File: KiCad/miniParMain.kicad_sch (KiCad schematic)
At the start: 37 parts, among them J1 Conn_01x08, J2 USB_C_Receptacle, J4 Conn_01x02_Pin, J5 secondBoard, SW2 SW_Push, U1 AS7341-DLGT, U2 IP4234CZ6, U5 AP7312-1833W6-7, U8 ESP8685, Y2 40MHz

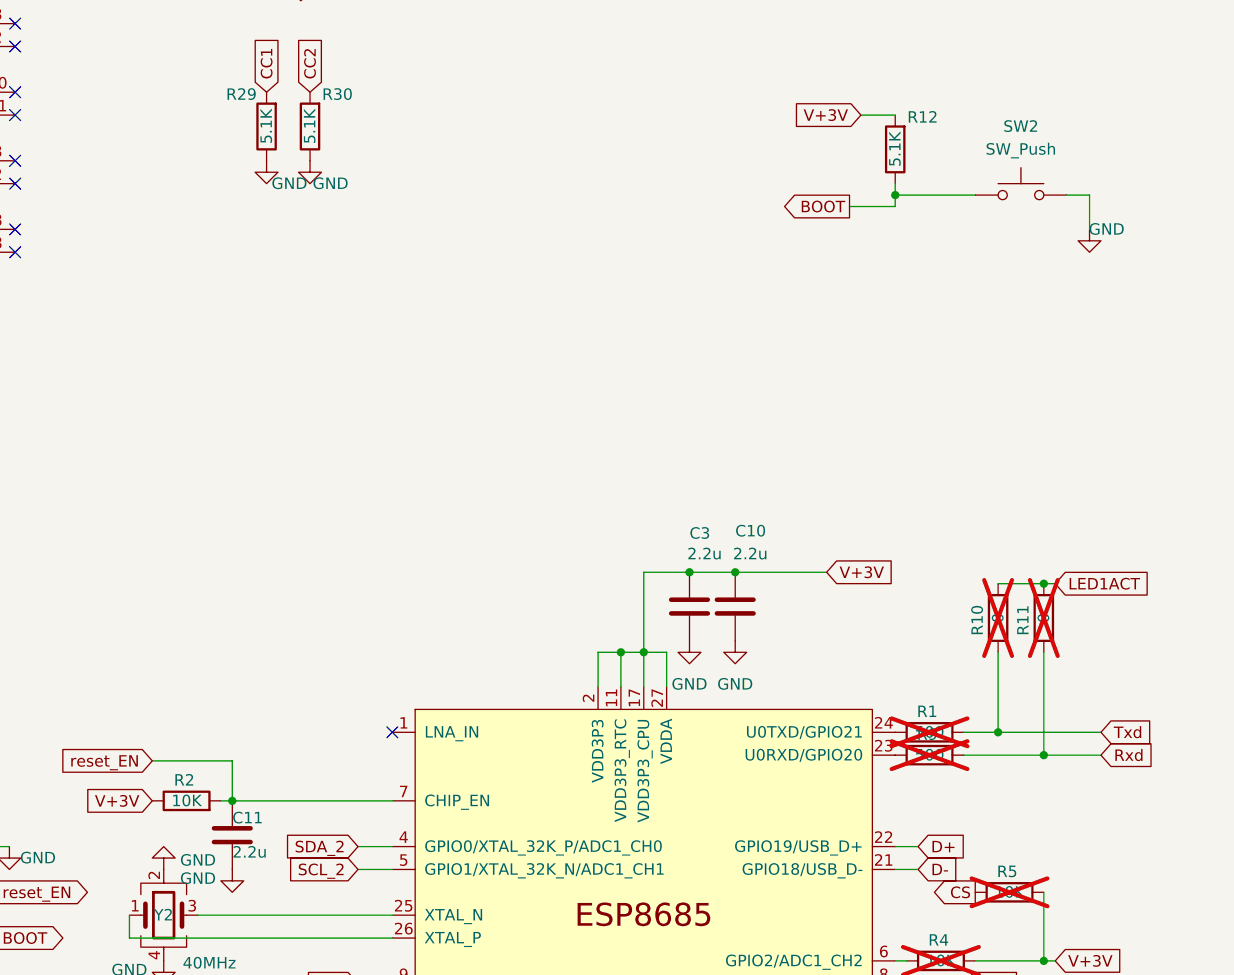
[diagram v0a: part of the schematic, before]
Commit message: clean up of schematics - mpn + bom
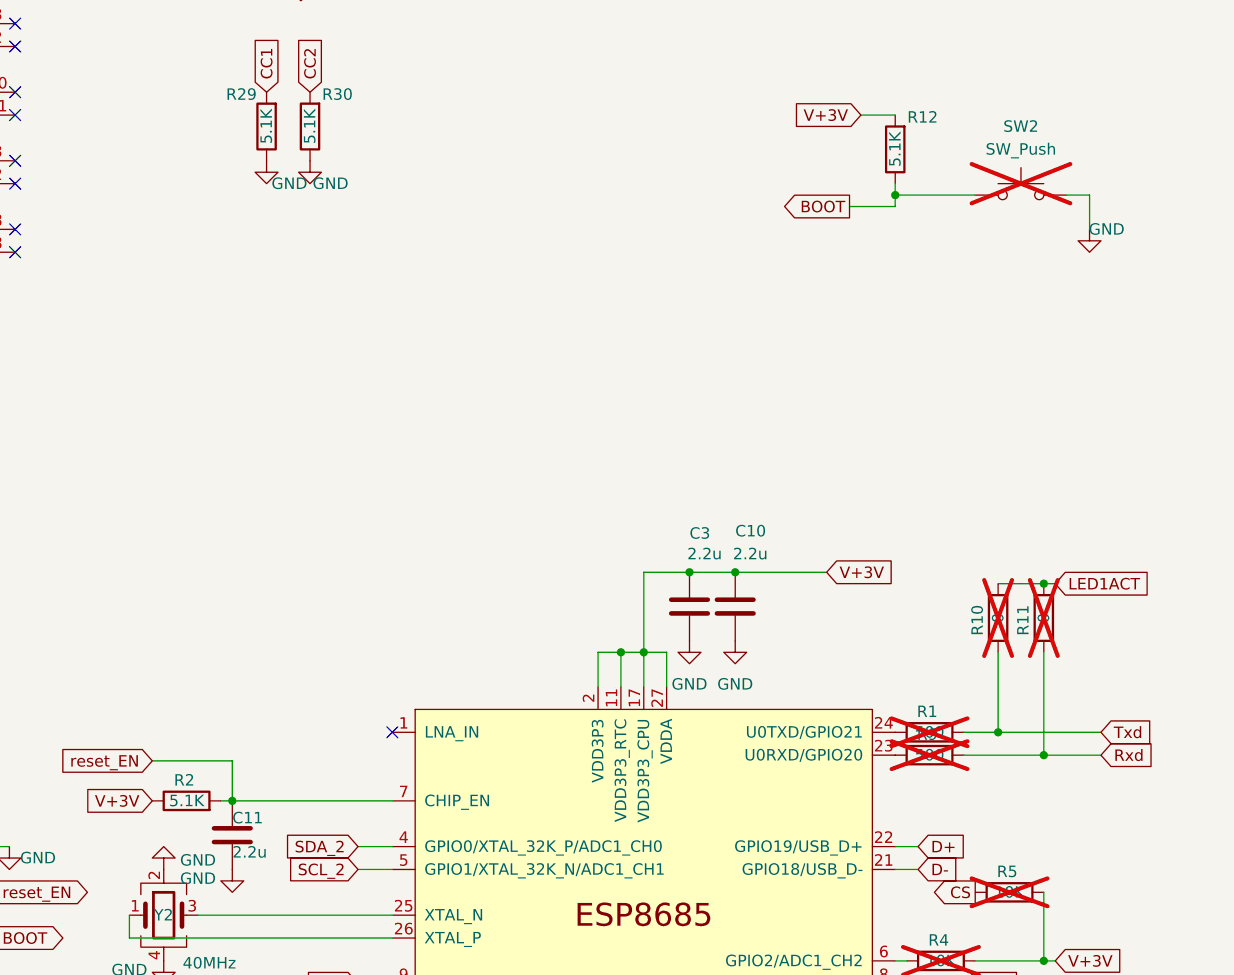
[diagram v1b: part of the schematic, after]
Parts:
- C1, C12: Manufacturer_Part_Number (none) -> GRT188R61H225KE13D
- C10, C11, C2, C3, C4, C9: MANUFACTURER CL05A225MQ5NNNC -> (none); Manufacturer_Part_Number (none) -> GRT188R61H225KE13D
- D1: Manufacturer_Part_Number (none) -> 1N4148W-TP
- D2, J1, J4, J5, R1, R10, R11, R3, R6, R7, R8, R9: now left out of the parts list
- D3: Manufacturer_Part_Number (none) -> LTST-C171KGKT
- R12, R13, R29, R30: Manufacturer_Part_Number RC1608J202CS -> 652-CR0603FX-5101ELF; manf# RC1608J202CS -> (none)
- R2: value 10K -> 5.1K; Manufacturer_Part_Number (none) -> 652-CR0603FX-5101ELF
- SW2: now not fitted; now left out of the parts list
- U1: Manufacturer_Part_Number (none) -> AS7341-DLGM
- U2: Manufacturer_Part_Number (none) -> IP4234CZ6,115
- U5: Manufacturer_Part_Number (none) -> AP7312-1833W6-7
- U8: Manufacturer_Part_Number (none) -> ESP8685H4
- Y2: Manufacturer_Part_Number (none) -> ECS-400-8-47B2-CKM-TR
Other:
- title: caliTool -> miniPAR
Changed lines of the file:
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@@
 	(paper "A4")
 	(title_block
-		(title "caliTool")
-		(date "2026-02-11")
-		(rev "0.1")
+		(title "miniPAR")
+		(date "2026-04-09")
+		(rev "1.1")
 		(company "JII")
 		(comment 1 "Łukasz Grabowski")
@@
 		(unit 1)
 		(exclude_from_sim no)
-		(in_bom yes)
+		(in_bom no)
 		(on_board yes)
 		(dnp yes)
@@
 			)
 		)
-		(property "Datasheet" "WR04X1002FTL"
+		(property "Datasheet" ""
 			(at 201.93 139.7 0)
 			(effects
@@
 			)
 		)
+		(property "Manufacturer_Part_Number" " LTST-C171KGKT"
+			(at 152.4 189.23 0)
+			(effects
+				(font
+					(size 1.27 1.27)
+				)
+				(hide yes)
+			)
+		)
 		(pin "2"
 		)
@@
 			)
 		)
-		(property "Datasheet" "RC1608J202CS"
+		(property "Datasheet" ""
 			(at 162.56 189.23 0)
 			(effects
@@
 			)
 		)
-		(property "manf#" "RC1608J202CS"
+		(property "manf#" ""
 			(at 162.56 189.23 0)
 			(effects
@@
 			)
 		)
-		(property "Manufacturer_Part_Number" "RC1608J202CS"
+		(property "Manufacturer_Part_Number" " 652-CR0603FX-5101ELF"
 			(at 162.56 189.23 0)
 			(effects
@@
 			)
 		)
-		(property "MANUFACTURER" "CL05A225MQ5NNNC"
+		(property "Manufacturer_Part_Number" "GRT188R61H225KE13D"
 			(at 67.31 161.29 0)
 			(effects
@@
 		(unit 1)
 		(exclude_from_sim no)
-		(in_bom yes)
+		(in_bom no)
 		(on_board no)
 		(dnp yes)
@@
 			)
 		)
+		(property "Manufacturer_Part_Number" " AS7341-DLGM"
+			(at 256.54 147.32 0)
+			(effects
+				(font
+					(size 1.27 1.27)
+				)
+				(hide yes)
+			)
+		)
 		(pin "1"
 		)
@@
 			)
 		)
-		(property "Datasheet" "https://www.diodes.com/assets/Datasheets/ds30396.pdf"
+		(property "Datasheet" "https://nl.mouser.com/ProductDetail/Micro-Commercial-Components-MCC/1N4148W-TP?qs=KFo7JewZbUH7wCMabJ4EeQ%3D%3D"
 			(at 72.39 21.59 0)
 			(effects
@@
 			)
 		)
+		(property "Manufacturer_Part_Number" " 1N4148W-TP"
+			(at 72.39 21.59 0)
+			(effects
+				(font
+					(size 1.27 1.27)
+				)
+				(hide yes)
+			)
+		)
 		(pin "2"
 		)
@@
 			)
 		)
+		(property "Manufacturer_Part_Number" " AP7312-1833W6-7"
+			(at 158.75 33.02 0)
+			(effects
+				(font
+					(size 1.27 1.27)
+				)
+				(hide yes)
+			)
+		)
 		(pin "2"
 		)
@@
 			)
 		)
-		(property "MANUFACTURER" "CL05A225MQ5NNNC"
+		(property "Manufacturer_Part_Number" "GRT188R61H225KE13D"
 			(at 193.04 41.91 0)
 			(effects
@@
 			)
 		)
+		(property "Manufacturer_Part_Number" " ECS-400-8-47B2-CKM-TR"
+			(at 59.69 170.18 0)
+			(effects
+				(font
+					(size 1.27 1.27)
+				)
+				(hide yes)
+			)
+		)
 		(pin "3"
 		)
@@
 		(unit 1)
 		(exclude_from_sim no)
-		(in_bom yes)
+		(in_bom no)
 		(on_board yes)
 		(dnp yes)
@@
 			)
 		)
-		(property "MANUFACTURER" "CL05A225MQ5NNNC"
+		(property "Manufacturer_Part_Number" "GRT188R61H225KE13D"
 			(at 175.26 41.91 0)
 			(effects
@@
 			)
 		)
+		(property "Manufacturer_Part_Number" " ESP8685H4"
+			(at 113.03 167.64 0)
+			(effects
+				(font
+					(size 1.27 1.27)
+				)
+				(hide yes)
+			)
+		)
 		(pin "26"
 		)
@@
 			)
 		)
-		(property "MANUFACTURER" "CL05A225MQ5NNNC"
+		(property "Manufacturer_Part_Number" "GRT188R61H225KE13D"
 			(at 236.22 146.05 0)
 			(effects
@@
 		(unit 1)
 		(exclude_from_sim no)
-		(in_bom yes)
+		(in_bom no)
 		(on_board yes)
 		(dnp yes)
@@
 		(unit 1)
 		(exclude_from_sim no)
-		(in_bom yes)
+		(in_bom no)
 		(on_board yes)
 		(dnp yes)
@@
 			)
 		)
-		(property "Datasheet" "WR04X1002FTL"
+		(property "Datasheet" ""
 			(at 203.2 156.21 0)
 			(effects
@@
 		(unit 1)
 		(exclude_from_sim no)
-		(in_bom yes)
+		(in_bom no)
 		(on_board yes)
 		(dnp yes)
@@
 			)
 		)
-		(property "Datasheet" "WR04X1002FTL"
+		(property "Datasheet" ""
 			(at 201.93 137.16 0)
 			(effects
@@
 		(unit 1)
 		(exclude_from_sim no)
-		(in_bom yes)
+		(in_bom no)
 		(on_board no)
 		(dnp yes)
@@
 			)
 		)
-		(property "MANUFACTURER" "CL05A225MQ5NNNC"
+		(property "Manufacturer_Part_Number" "GRT188R61H225KE13D"
 			(at 118.11 135.89 0)
 			(effects
@@
 		(unit 1)
 		(exclude_from_sim no)
-		(in_bom yes)
+		(in_bom no)
 		(on_board no)
 		(dnp yes)
@@
 		(unit 1)
 		(exclude_from_sim no)
-		(in_bom yes)
+		(in_bom no)
 		(on_board no)
 		(dnp yes)
@@
 			)
 		)
-		(property "Datasheet" "CR0402-JW-511GLF"
+		(property "Datasheet" ""
 			(at 144.78 149.86 0)
 			(effects
@@
 			)
 		)
-		(property "MANUFACTURER" "CL05A225MQ5NNNC"
+		(property "Manufacturer_Part_Number" "GRT188R61H225KE13D"
 			(at 123.19 135.89 0)
 			(effects
@@
 			)
 		)
+		(property "Manufacturer_Part_Number" " IP4234CZ6,115"
+			(at 74.93 53.34 0)
+			(effects
+				(font
+					(size 1.27 1.27)
+				)
+				(hide yes)
+			)
+		)
 		(pin "5"
 		)
@@
 			)
 		)
+		(property "Manufacturer_Part_Number" "GRT188R61H225KE13D"
+			(at 140.97 40.64 0)
+			(effects
+				(font
+					(size 1.27 1.27)
+				)
+				(hide yes)
+			)
+		)
 		(pin "1"
 		)
@@
 			)
 		)
-		(property "Datasheet" "RC1608J202CS"
+		(property "Datasheet" ""
 			(at 140.97 85.09 0)
 			(effects
@@
 			)
 		)
-		(property "manf#" "RC1608J202CS"
-			(at 140.97 85.09 0)
-			(effects
-				(font
-					(size 1.524 1.524)
-				)
-				(hide yes)
-			)
-		)
 		(property "price 10" ""
 			(at 140.97 85.09 0)
@@
 			)
 		)
-		(property "Manufacturer_Part_Number" "RC1608J202CS"
+		(property "Manufacturer_Part_Number" " 652-CR0603FX-5101ELF"
 			(at 140.97 85.09 0)
 			(effects
@@
 			)
 		)
-		(property "Datasheet" "RC1608J202CS"
+		(property "Datasheet" ""
 			(at 75.946 82.55 0)
 			(effects
@@
 			)
 		)
-		(property "manf#" "RC1608J202CS"
-			(at 75.946 82.55 0)
-			(effects
-				(font
-					(size 1.524 1.524)
-				)
-				(hide yes)
-			)
-		)
 		(property "price 10" ""
 			(at 75.946 82.55 0)
@@
 			)
 		)
-		(property "Manufacturer_Part_Number" "RC1608J202CS"
+		(property "Manufacturer_Part_Number" " 652-CR0603FX-5101ELF"
 			(at 75.946 82.55 0)
 			(effects
@@
 		(unit 1)
 		(exclude_from_sim no)
-		(in_bom yes)
+		(in_bom no)
 		(on_board no)
 		(dnp yes)
@@
 			)
 		)
-		(property "Datasheet" "CR0402-JW-511GLF"
+		(property "Datasheet" ""
 			(at 144.78 152.4 0)
 			(effects
@@
 		(unit 1)
 		(exclude_from_sim no)
-		(in_bom yes)
+		(in_bom no)
 		(on_board yes)
-		(dnp no)
+		(dnp yes)
 		(fields_autoplaced yes)
 		(property "Reference" "SW2"
@@
 		(unit 1)
 		(exclude_from_sim no)
-		(in_bom yes)
+		(in_bom no)
 		(on_board yes)
 		(dnp yes)
@@
 			)
 		)
+		(property "Manufacturer_Part_Number" "GRT188R61H225KE13D"
+			(at 104.14 25.4 0)
+			(effects
+				(font
+					(size 1.27 1.27)
+				)
+				(hide yes)
+			)
+		)
 		(pin "1"
 		)
@@
 		(unit 1)
 		(exclude_from_sim no)
-		(in_bom yes)
+		(in_bom no)
 		(on_board yes)
 		(dnp yes)
@@
 			)
 		)
-		(property "Datasheet" "WR04X1002FTL"
+		(property "Datasheet" ""
 			(at 203.2 160.02 0)
 			(effects
@@
 			)
 		)
-		(property "Value" "10K"
+		(property "Value" "5.1K"
 			(at 62.23 157.48 90)
 			(effects
@@
 			)
 		)
-		(property "Datasheet" "WR04X1002FTL"
+		(property "Datasheet" ""
 			(at 62.23 157.48 0)
 			(effects
@@
 			)
 		)
+		(property "Manufacturer_Part_Number" " 652-CR0603FX-5101ELF"
+			(at 62.23 157.48 90)
+			(effects
+				(font
+					(size 1.27 1.27)
+				)
+				(hide yes)
+			)
+		)
 		(pin "1"
 		)
@@
 			)
 		)
-		(property "Datasheet" "RC1608J202CS"
+		(property "Datasheet" ""
 			(at 71.12 82.55 0)
 			(effects
@@
 			)
 		)
-		(property "manf#" "RC1608J202CS"
+		(property "manf#" ""
 			(at 71.12 82.55 0)
 			(effects
@@
 			)
 		)
-		(property "Manufacturer_Part_Number" "RC1608J202CS"
+		(property "Manufacturer_Part_Number" " 652-CR0603FX-5101ELF"
 			(at 71.12 82.55 0)
 			(effects
@@
 			)
 		)
-		(property "Datasheet" "WR04X1002FTL"
+		(property "Datasheet" ""
 			(at 153.67 167.64 0)
 			(effects
@@
 			)
 		)
-		(property "Datasheet" "WR04X1002FTL"
+		(property "Datasheet" ""
 			(at 146.05 175.26 0)
 			(effects
